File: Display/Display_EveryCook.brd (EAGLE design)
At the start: 82.3 x 41.3 mm, 130 parts

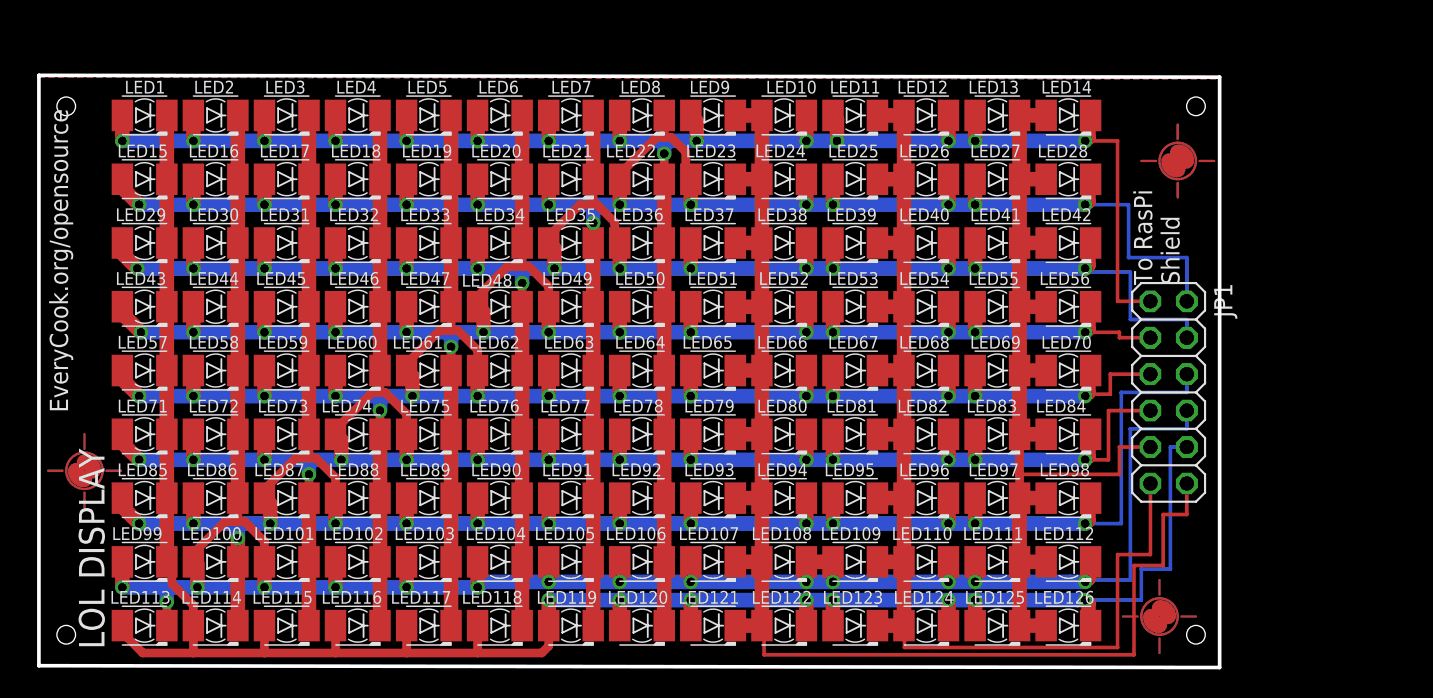
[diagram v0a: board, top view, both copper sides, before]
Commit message: Changed USB connectors, created gerber Files
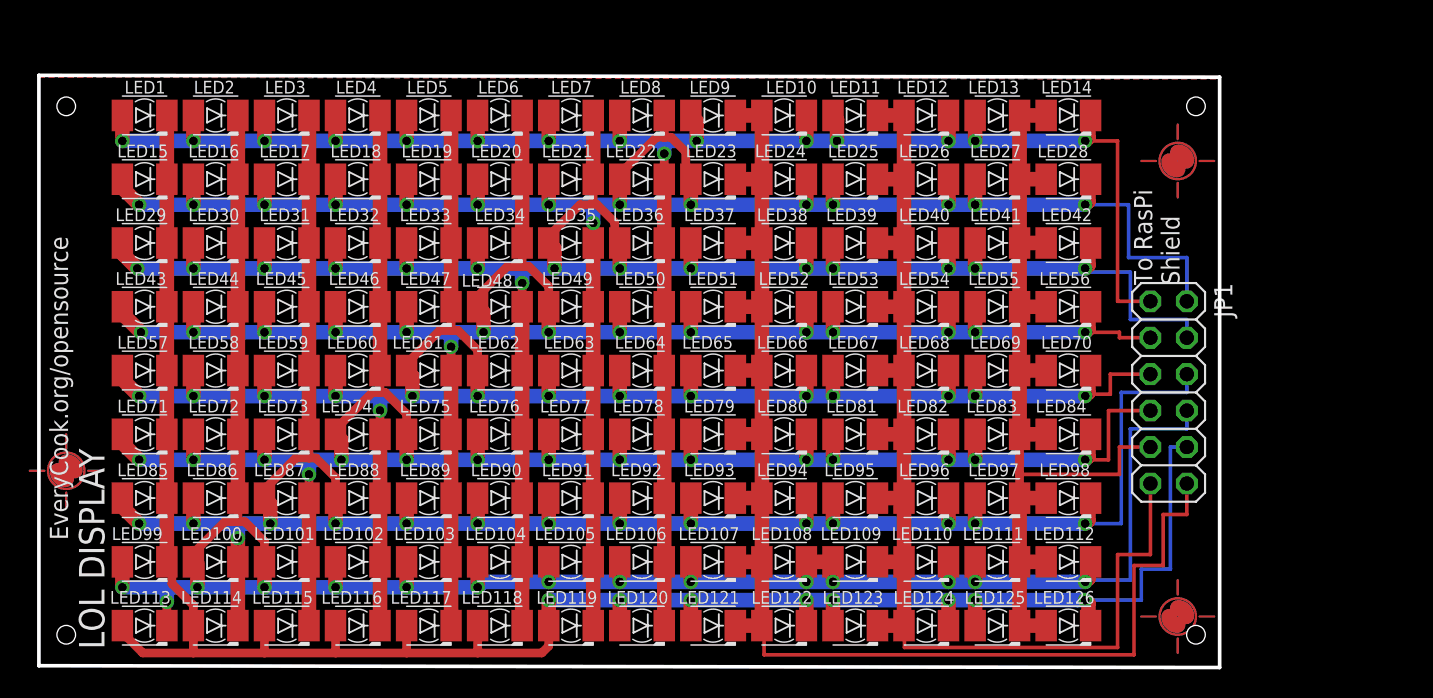
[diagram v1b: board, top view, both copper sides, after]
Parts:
- moved U$3 1.27 mm to (74.9, 8.89)
- moved U$2 1.27 mm to (-2.54, 19.1)
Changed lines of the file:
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@@
 <wire x1="-4.445" y1="46.609" x2="77.851" y2="46.482" width="0.254" layer="20"/>
 <wire x1="-4.445" y1="46.609" x2="-4.445" y2="5.461" width="0.254" layer="20"/>
-<text x="-2.413" y="23.114" size="1.27" layer="21" ratio="20" rot="R90">EveryCook.org/opensource</text>
+<text x="-2.413" y="14.224" size="1.27" layer="21" ratio="20" rot="R90">EveryCook.org/opensource</text>
 <text x="68.453" y="46.355" size="1.016" layer="27" ratio="20">+</text>
 <text x="68.58" y="51.943" size="1.016" layer="27" ratio="20">-</text>
@@
 <element name="JP1" library="pinhead" package="2X06" value="" x="74.295" y="24.511" rot="R270"/>
 <element name="U$1" library="marks" package="PASS-ROUND" value="" x="74.93" y="40.64"/>
-<element name="U$2" library="marks" package="PASS-ROUND" value="" x="-1.27" y="19.05"/>
-<element name="U$3" library="marks" package="PASS-ROUND" value="" x="73.66" y="8.89"/>
+<element name="U$2" library="marks" package="PASS-ROUND" value="" x="-2.54" y="19.05"/>
+<element name="U$3" library="marks" package="PASS-ROUND" value="" x="74.93" y="8.89"/>
 </elements>
 <signals>

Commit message: Redesign of all boards.
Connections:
- removed net N$5: JP1.12, LED10.A, LED107.C, LED108.A, LED121.C, LED122.A, LED23.C, LED24.A, LED37.C, LED38.A, LED51.C, LED52.A, LED65.C, LED66.A, LED79.C, LED80.A, LED9.C, LED93.C, LED94.A
- removed net PIN10: JP1.3, LED103.C, LED117.C, LED20.C, LED34.C, LED43.A, LED44.A, LED45.A, LED46.A, LED47.A, LED48.A, LED49.A, LED50.A, LED51.A, LED52.C, LED53.A, LED54.C, LED55.A, LED56.C, LED6.C, LED61.C, LED75.C, LED89.C
- removed net PIN11: JP1.4, LED104.C, LED118.C, LED21.C, LED29.A, LED30.A, LED31.A, LED32.A, LED33.A, LED34.A, LED35.A, LED36.A, LED37.A, LED38.C, LED39.A, LED40.C, LED41.A, LED42.C, LED48.C, LED62.C, LED7.C, LED76.C, LED90.C
- removed net PIN12: JP1.2, LED105.C, LED119.C, LED15.A, LED16.A, LED17.A, LED18.A, LED19.A, LED20.A, LED21.A, LED22.A, LED23.A, LED24.C, LED25.A, LED26.C, LED27.A, LED28.C, LED35.C, LED49.C, LED63.C, LED77.C, LED8.C, LED91.C
- removed net PIN13: JP1.1, LED1.A, LED10.C, LED106.C, LED11.A, LED12.C, LED120.C, LED13.A, LED14.C, LED2.A, LED22.C, LED3.A, LED36.C, LED4.A, LED5.A, LED50.C, LED6.A, LED64.C, LED7.A, LED78.C, LED8.A, LED9.A, LED92.C
- removed net PIN2: JP1.9, LED111.C, LED112.A, LED125.C, LED126.A, LED13.C, LED14.A, LED27.C, LED28.A, LED41.C, LED42.A, LED55.C, LED56.A, LED69.C, LED70.A, LED83.C, LED84.A, LED97.C, LED98.A
- removed net PIN3: JP1.11, LED109.C, LED11.C, LED110.A, LED12.A, LED123.C, LED124.A, LED25.C, LED26.A, LED39.C, LED40.A, LED53.C, LED54.A, LED67.C, LED68.A, LED81.C, LED82.A, LED95.C, LED96.A
- removed net PIN5: JP1.10, LED1.C, LED113.A, LED114.A, LED115.A, LED116.A, LED117.A, LED118.A, LED119.A, LED120.A, LED121.A, LED122.C, LED123.A, LED124.C, LED125.A, LED126.C, LED15.C, LED29.C, LED43.C, LED57.C, LED71.C, LED85.C, LED99.C
- removed net PIN6: JP1.8, LED100.A, LED101.A, LED102.A, LED103.A, LED104.A, LED105.A, LED106.A, LED107.A, LED108.C, LED109.A, LED110.C, LED111.A, LED112.C, LED113.C, LED16.C, LED2.C, LED30.C, LED44.C, LED58.C, LED72.C, LED86.C, LED99.A
- removed net PIN7: JP1.6, LED100.C, LED114.C, LED17.C, LED3.C, LED31.C, LED45.C, LED59.C, LED73.C, LED85.A, LED86.A, LED87.A, LED88.A, LED89.A, LED90.A, LED91.A, LED92.A, LED93.A, LED94.C, LED95.A, LED96.C, LED97.A, LED98.C
- removed net PIN8: JP1.7, LED101.C, LED115.C, LED18.C, LED32.C, LED4.C, LED46.C, LED60.C, LED71.A, LED72.A, LED73.A, LED74.A, LED75.A, LED76.A, LED77.A, LED78.A, LED79.A, LED80.C, LED81.A, LED82.C, LED83.A, LED84.C, LED87.C
- removed net PIN9: JP1.5, LED102.C, LED116.C, LED19.C, LED33.C, LED47.C, LED5.C, LED57.A, LED58.A, LED59.A, LED60.A, LED61.A, LED62.A, LED63.A, LED64.A, LED65.A, LED66.C, LED67.A, LED68.C, LED69.A, LED70.C, LED74.C, LED88.C
- new net PB0: JP1.1, LED103.C, LED117.C, LED20.C, LED34.C, LED43.A, LED44.A, LED45.A, LED46.A, LED47.A, LED48.A, LED49.A, LED50.A, LED51.A, LED52.C, LED53.A, LED54.C, LED55.A, LED56.C, LED6.C, LED61.C, LED75.C, LED89.C
- new net PB1: JP1.2, LED104.C, LED118.C, LED21.C, LED29.A, LED30.A, LED31.A, LED32.A, LED33.A, LED34.A, LED35.A, LED36.A, LED37.A, LED38.C, LED39.A, LED40.C, LED41.A, LED42.C, LED48.C, LED62.C, LED7.C, LED76.C, LED90.C
- new net PB2: JP1.3, LED105.C, LED119.C, LED15.A, LED16.A, LED17.A, LED18.A, LED19.A, LED20.A, LED21.A, LED22.A, LED23.A, LED24.C, LED25.A, LED26.C, LED27.A, LED28.C, LED35.C, LED49.C, LED63.C, LED77.C, LED8.C, LED91.C
- new net PB3: JP1.4, LED1.A, LED10.C, LED106.C, LED11.A, LED12.C, LED120.C, LED13.A, LED14.C, LED2.A, LED22.C, LED3.A, LED36.C, LED4.A, LED5.A, LED50.C, LED6.A, LED64.C, LED7.A, LED78.C, LED8.A, LED9.A, LED92.C
- new net PC0: JP1.5, LED111.C, LED112.A, LED125.C, LED126.A, LED13.C, LED14.A, LED27.C, LED28.A, LED41.C, LED42.A, LED55.C, LED56.A, LED69.C, LED70.A, LED83.C, LED84.A, LED97.C, LED98.A
- new net PC1: JP1.6, LED109.C, LED11.C, LED110.A, LED12.A, LED123.C, LED124.A, LED25.C, LED26.A, LED39.C, LED40.A, LED53.C, LED54.A, LED67.C, LED68.A, LED81.C, LED82.A, LED95.C, LED96.A
- new net PC2: JP1.7, LED10.A, LED107.C, LED108.A, LED121.C, LED122.A, LED23.C, LED24.A, LED37.C, LED38.A, LED51.C, LED52.A, LED65.C, LED66.A, LED79.C, LED80.A, LED9.C, LED93.C, LED94.A
- new net PC3: JP1.8, LED1.C, LED113.A, LED114.A, LED115.A, LED116.A, LED117.A, LED118.A, LED119.A, LED120.A, LED121.A, LED122.C, LED123.A, LED124.C, LED125.A, LED126.C, LED15.C, LED29.C, LED43.C, LED57.C, LED71.C, LED85.C, LED99.C
- new net PC4: JP1.9, LED100.A, LED101.A, LED102.A, LED103.A, LED104.A, LED105.A, LED106.A, LED107.A, LED108.C, LED109.A, LED110.C, LED111.A, LED112.C, LED113.C, LED16.C, LED2.C, LED30.C, LED44.C, LED58.C, LED72.C, LED86.C, LED99.A
- new net PC5: JP1.10, LED100.C, LED114.C, LED17.C, LED3.C, LED31.C, LED45.C, LED59.C, LED73.C, LED85.A, LED86.A, LED87.A, LED88.A, LED89.A, LED90.A, LED91.A, LED92.A, LED93.A, LED94.C, LED95.A, LED96.C, LED97.A, LED98.C
- new net PC6: JP1.11, LED101.C, LED115.C, LED18.C, LED32.C, LED4.C, LED46.C, LED60.C, LED71.A, LED72.A, LED73.A, LED74.A, LED75.A, LED76.A, LED77.A, LED78.A, LED79.A, LED80.C, LED81.A, LED82.C, LED83.A, LED84.C, LED87.C
- new net PC7: JP1.12, LED102.C, LED116.C, LED19.C, LED33.C, LED47.C, LED5.C, LED57.A, LED58.A, LED59.A, LED60.A, LED61.A, LED62.A, LED63.A, LED64.A, LED65.A, LED66.C, LED67.A, LED68.C, LED69.A, LED70.C, LED74.C, LED88.C
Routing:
- net PC3: track 0.00 -> 153.7 mm, vias 0 -> 8
- net PIN6: track 150.5 -> 0.00 mm, vias 15 -> 0
- net PIN7: track 148.6 -> 0.00 mm, vias 15 -> 0
- net PIN5: track 148.3 -> 0.00 mm, vias 8 -> 0
- net PB3: track 0.00 -> 147.0 mm, vias 0 -> 15
- net PC5: track 0.00 -> 146.0 mm, vias 0 -> 15
- net PC4: track 0.00 -> 145.4 mm, vias 0 -> 15
- net PB2: track 0.00 -> 145.2 mm, vias 0 -> 15
- net PIN12: track 144.6 -> 0.00 mm, vias 15 -> 0
- net PC7: track 0.00 -> 144.1 mm, vias 0 -> 15
- net PIN11: track 142.8 -> 0.00 mm, vias 15 -> 0
- net PIN13: track 141.9 -> 0.00 mm, vias 15 -> 0
- net PB1: track 0.00 -> 140.3 mm, vias 0 -> 15
- net PB0: track 0.00 -> 139.0 mm, vias 0 -> 15
- net PIN8: track 138.9 -> 0.00 mm, vias 15 -> 0
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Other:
- board text added: "1"
- board text added: "2"
- board text added: "PB0"
- board text added: "PB1"
- board text added: "PB2"
- board text added: "PB3"
- board text added: "PC0"
- board text added: "PC1"
- board text added: "PC2"
- board text added: "PC3"
- board text added: "PC4"
- board text added: "PC5"
- board text added: "PC6"
- board text added: "PC7"
